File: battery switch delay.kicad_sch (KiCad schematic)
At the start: 11 parts, among them J1 5mm pitch 4 position screw te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, K2 G6E-134P-US, Q1 Q_NPN, U2 MIC2920A-12WS-TR_SOT223

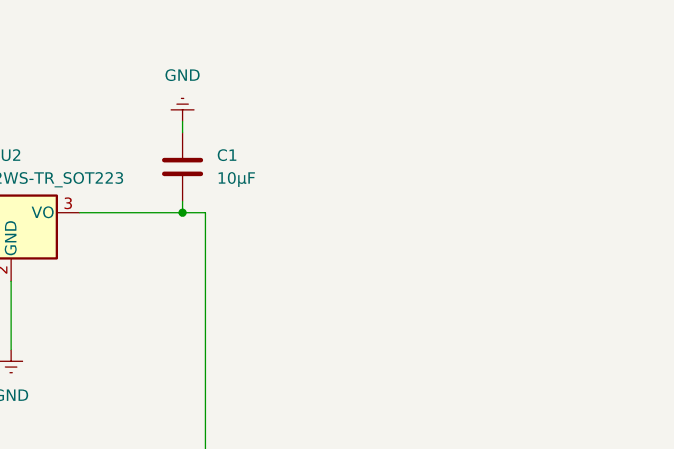
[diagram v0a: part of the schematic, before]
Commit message: changed the cap on the voltage regulator in the schematic and baord
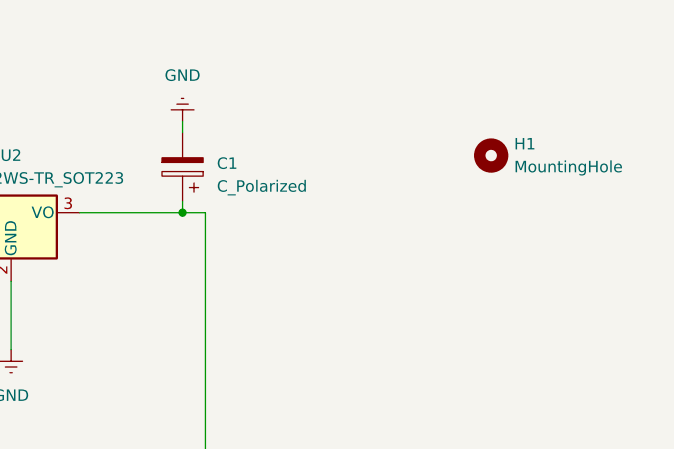
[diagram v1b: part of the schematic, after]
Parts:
- removed C1: 10μF, Capacitor_SMD:C_0805_2012Metric_Pad1.18x1.45mm_HandSolder, symbol Device:C
- added C1: C_Polarized, symbol Device:C_Polarized
- added H1: MountingHole, symbol Mechanical:MountingHole
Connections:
- net GND: now also C1.2
- net at A1.30 (VIN), U2.3 (VO): now also C1.1
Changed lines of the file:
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@@
+	)
+	(symbol
+		(lib_id "Mechanical:MountingHole")
+		(at 179.07 29.21 0)
+		(unit 1)
+		(exclude_from_sim no)
+		(in_bom no)
+		(on_board yes)
+		(dnp no)
+		(fields_autoplaced yes)
+		(property "Reference" "H1"
+			(at 181.61 27.9399 0)
+			(effects
+				(font
+					(size 1.27 1.27)
+				)
+				(justify left)
+			)
+		)
+		(property "Value" "MountingHole"
+			(at 181.61 30.4799 0)
+			(effects
+				(font
+					(size 1.27 1.27)
+				)
+				(justify left)
+			)
+		)
+		(property "Footprint" ""
+			(at 179.07 29.21 0)
+			(effects
+				(font
+					(size 1.27 1.27)
+				)
+				(hide yes)
+			)
+		)
+		(property "Datasheet" "~"
+			(at 179.07 29.21 0)
+			(effects
+				(font
+					(size 1.27 1.27)
+				)
+				(hide yes)
+			)
+		)
+		(property "Description" "Mounting Hole without connection"
+			(at 179.07 29.21 0)
+			(effects
+				(font
+					(size 1.27 1.27)
+				)
+				(hide yes)
+			)
+		)
+		(instances
+			(project ""
+				(path "/72486ea4-2971-4ca2-ab8b-187d20cf76b7"
+					(reference "H1")
+					(unit 1)
+				)
+			)
+		)
 	)
 	(symbol
@@
 				(path "/72486ea4-2971-4ca2-ab8b-187d20cf76b7"
 					(reference "#PWR05")
-					(unit 1)
-				)
-			)
-		)
-	)
-	(symbol
-		(lib_id "Device:C")
-		(at 144.78 30.48 180)
-		(unit 1)
-		(exclude_from_sim no)
-		(in_bom yes)
-		(on_board yes)
-		(dnp no)
-		(fields_autoplaced yes)
-		(property "Reference" "C1"
-			(at 148.59 29.2099 0)
-			(effects
-				(font
-					(size 1.27 1.27)
-				)
-				(justify right)
-			)
-		)
-		(property "Value" "10μF"
-			(at 148.59 31.7499 0)
-			(effects
-				(font
-					(size 1.27 1.27)
-				)
-				(justify right)
-			)
-		)
-		(property "Footprint" "Capacitor_SMD:C_0805_2012Metric_Pad1.18x1.45mm_HandSolder"
-			(at 143.8148 26.67 0)
-			(effects
-				(font
-					(size 1.27 1.27)
-				)
-				(hide yes)
-			)
-		)
-		(property "Datasheet" "~"
-			(at 144.78 30.48 0)
-			(effects
-				(font
-					(size 1.27 1.27)
-				)
-				(hide yes)
-			)
-		)
-		(property "Description" "Unpolarized capacitor, rated for 40v"
-			(at 144.78 30.48 0)
-			(effects
-				(font
-					(size 1.27 1.27)
-				)
-				(hide yes)
-			)
-		)
-		(pin "2"
-		)
-		(pin "1"
-		)
-		(instances
-			(project ""
-				(path "/72486ea4-2971-4ca2-ab8b-187d20cf76b7"
-					(reference "C1")
 					(unit 1)
 				)
@@
 					(unit 1)
 				)
+			)
+		)
+	)
+	(symbol
+		(lib_id "Device:C_Polarized")
+		(at 144.78 30.48 180)
+		(unit 1)
+		(exclude_from_sim no)
+		(in_bom yes)
+		(on_board yes)
+		(dnp no)
+		(fields_autoplaced yes)
+		(property "Reference" "C1"
+			(at 148.59 30.0989 0)
+			(effects
+				(font
+					(size 1.27 1.27)
+				)
+				(justify right)
+			)
+		)
+		(property "Value" "C_Polarized"
+			(at 148.59 32.6389 0)
+			(effects
+				(font
+					(size 1.27 1.27)
+				)
+				(justify right)
+			)
+		)
+		(property "Footprint" ""
+			(at 143.8148 26.67 0)
+			(effects
+				(font
+					(size 1.27 1.27)
+				)
+				(hide yes)
+			)
+		)
+		(property "Datasheet" "~"
+			(at 144.78 30.48 0)
+			(effects
+				(font
+					(size 1.27 1.27)
+				)
+				(hide yes)
+			)
+		)
+		(property "Description" "Polarized capacitor"
+			(at 144.78 30.48 0)
+			(effects
+				(font
+					(size 1.27 1.27)
+				)
+				(hide yes)
+			)
+		)
+		(pin "1"
+		)
+		(pin "2"
+		)
+		(instances
+			(project ""
+				(path "/72486ea4-2971-4ca2-ab8b-187d20cf76b7"
+					(reference "C1")
+					(unit 1)
+				)

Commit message: more rand changes ig
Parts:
- removed H1: MountingHole, symbol Mechanical:MountingHole
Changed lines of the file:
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@@
-	)
-	(symbol
-		(lib_id "Mechanical:MountingHole")
-		(at 179.07 29.21 0)
-		(unit 1)
-		(exclude_from_sim no)
-		(in_bom no)
-		(on_board yes)
-		(dnp no)
-		(fields_autoplaced yes)
-		(property "Reference" "H1"
-			(at 181.61 27.9399 0)
-			(effects
-				(font
-					(size 1.27 1.27)
-				)
-				(justify left)
-			)
-		)
-		(property "Value" "MountingHole"
-			(at 181.61 30.4799 0)
-			(effects
-				(font
-					(size 1.27 1.27)
-				)
-				(justify left)
-			)
-		)
-		(property "Footprint" ""
-			(at 179.07 29.21 0)
-			(effects
-				(font
-					(size 1.27 1.27)
-				)
-				(hide yes)
-			)
-		)
-		(property "Datasheet" "~"
-			(at 179.07 29.21 0)
-			(effects
-				(font
-					(size 1.27 1.27)
-				)
-				(hide yes)
-			)
-		)
-		(property "Description" "Mounting Hole without connection"
-			(at 179.07 29.21 0)
-			(effects
-				(font
-					(size 1.27 1.27)
-				)
-				(hide yes)
-			)
-		)
-		(instances
-			(project ""
-				(path "/72486ea4-2971-4ca2-ab8b-187d20cf76b7"
-					(reference "H1")
-					(unit 1)
-				)
-			)
-		)
 	)
 	(symbol
